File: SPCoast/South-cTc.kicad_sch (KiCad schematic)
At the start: 6 parts

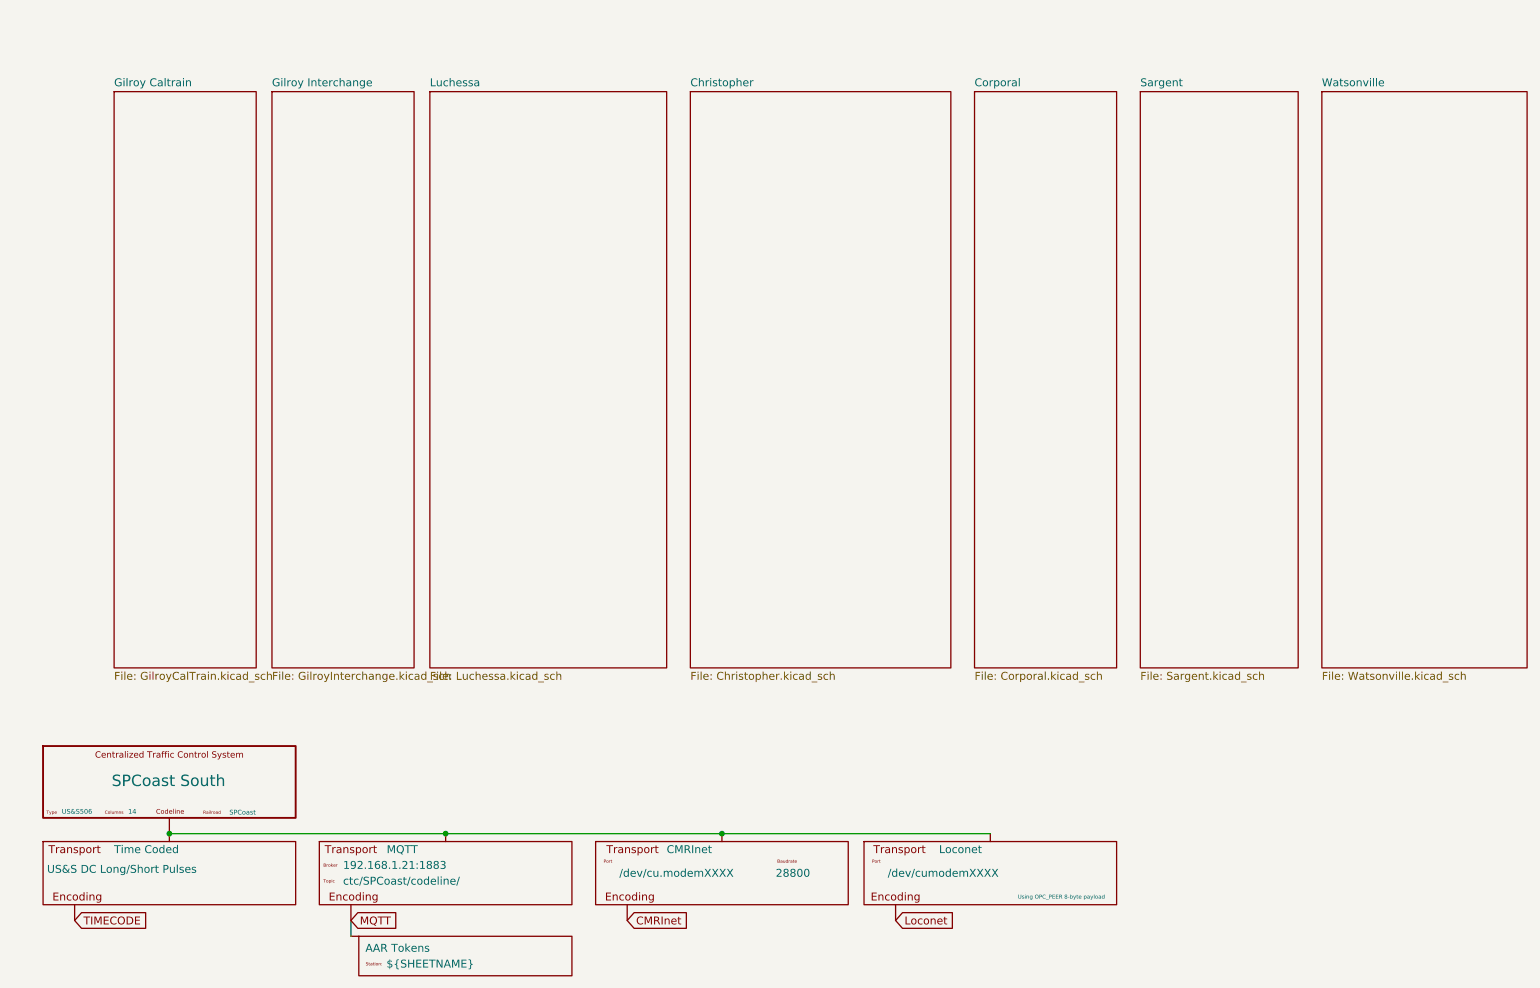
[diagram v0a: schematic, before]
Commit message: chore(kicad): owner mockup: explicit seam wiring on Luchessa and South-cTc, host and bus pins
Owner's edits, committed as they stand (2026-10-21), before scripted edits build on them.

- Interlocking gains Codeline and Host pins; MAIN HOUSE's Interlocking pin is Codeline.
- OfficeUnit gains Host and Codeline pins; JohnCTC desk processor drawn on South-cTc.
- Processor gains Transport and IO pins; MAX7313 and MCP23017 gain an I2C bus pin.
- Transports: Codeline pin renamed Host; JMRI_MQTT instance added; Loconet removed.
- Encodings' pin renamed Transport; Luchessa's 506 and Bit Packing instances removed.
- SPCoastApp virtual host (FieldUnit_Virtual) hosts CMRInet and JMRI_MQTT.
- Luchessa: unit, houses and Time Coded on one net; Host to its own processor;
  panel MAX7313s on the desk bus (OfficeBus).
- Watsonville, Caltrain, Interchange: first-pass Processor placeholders, to be redrawn.

Verified: netlist and ERC exported from the saved project; field diff against the
committed netlist shows no per-instance field lost.
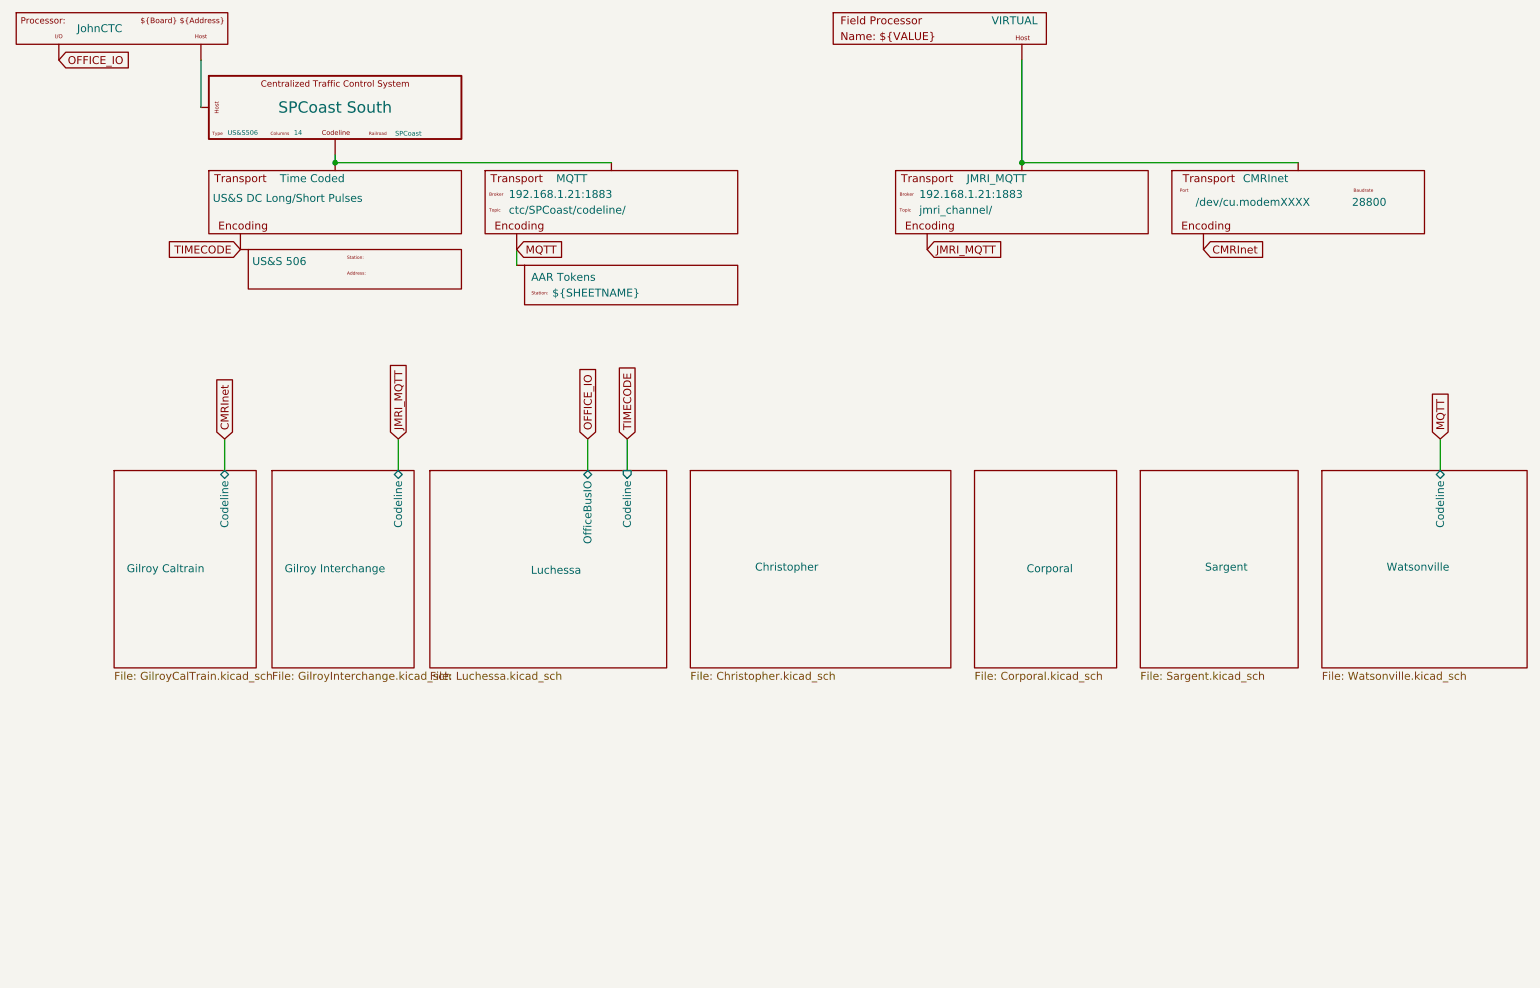
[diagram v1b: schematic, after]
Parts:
- removed Transport2008: Loconet, symbol Railroad-Office:Codeline-Transport-Loconet
- added Encoding2: US&S 506, symbol Railroad-Office:Codeline-Encoding-US&S-506
- added HOST1: SPCoastApp, symbol Railroad-Office:FieldUnit_Virtual
- added Proc4: JohnCTC, symbol Railroad-HardwareIO:Processor
- added Transport2009: JMRI_MQTT, symbol Railroad-Office:Codeline-Transport-MQTT
- MACHINE2002: symbol Railroad-Office:CtcMachine -> Railroad-Office:OfficeUnit
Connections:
- net TIMECODE: now also Encoding2.1 (Transport)
- net at MACHINE2002.1 (Codeline), Transport2005.1 (Host), Transport2006.1 (Host): no longer Transport2007.1 (Codeline)
- new net: MACHINE2002. (Host), Proc4.1 (Transport)
- new net: HOST1.1 (Host), Transport2007.1 (Host), Transport2009.1 (Host)
- new net JMRI_MQTT: Transport2009.2 (Encoding)
- new net OFFICE_IO: Proc4.2 (IO)
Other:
- sheet Gilroy Caltrain ports: added Codeline; removed none
- sheet Gilroy Interchange ports: added Codeline; removed none
- sheet Luchessa ports: added Codeline, OfficeBusIO; removed none
- sheet Watsonville ports: added Codeline; removed none
